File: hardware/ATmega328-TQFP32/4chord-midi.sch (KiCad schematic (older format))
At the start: 55 parts, among them IC1 ATMEGA328P-A, P1 USB_B, P2 Programmer, P3 UART, Q1 2N2222, SW1 Menu Minus, SW2 Menu Select, SW3 Menu Plus, SW4 Chord I, SW5 Chord V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

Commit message: issue-#13: Revised Revision B hardware
Reworked schematic to separate to logical blocks, added reset circuit,
fixed Q1 pin assignment and changed it from BJT to MOSFET component.
Also added power supply choices for UART (5V, 3.3V and none) and a
fourth rubber foot for better balance.

Obviously same changes in the PCB design, also moved button silk screen
bit more down for better readability. Fixed one sharp corner in the
board border. Improved routing somewhat.
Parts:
- removed Q1: 2N2222, TO_SOT_Packages_SMD:SOT-23, symbol Q_NPN_EBC
- removed R19, R20: 0R, Resistors_SMD:R_0805_HandSoldering, symbol R
- removed W1: TP, Pin_Headers:Pin_Header_Straight_1x01_Pitch2.54mm, symbol TEST_1P
- added C16: 100n, Capacitors_SMD:C_0805_HandSoldering, symbol C
- added P4: UART Power, Pin_Headers:Pin_Header_Straight_1x04_Pitch2.54mm, symbol CONN_01X04
- added Q1: 2N7002, TO_SOT_Packages_SMD:SOT-23, symbol Q_NMOS_GSD
- R16: value 1k -> 100
- R17: value 0R -> 1M
- R18: value 0R -> 10k
- SW1: value Menu Minus -> <
- SW2: value Menu Select -> Select
- SW3: value Menu Plus -> >
- SW4: value Chord I -> I
- SW5: value Chord V -> V
- SW6: value Chord vi -> vi
- SW7: value Chord IV -> IV
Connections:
- net labels added: +5V, BTN_MENU_NEXT, BTN_MENU_PREV
- net labels removed: BTN_MENU_MINUS, BTN_MENU_PLUS
- wire segments 166 -> 170
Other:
- note added: "Chord buttons"
- note added: "Clock"
- note added: "LCD / back light"
- note added: "Menu buttons"
- note added: "Power"
- note added: "Serial Programmer"
- note added: "UART"
- note added: "USB"
- moved on the sheet: C1, C10, C11, C12, C13, C14, C15, C2, C3, C4, C5, C6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

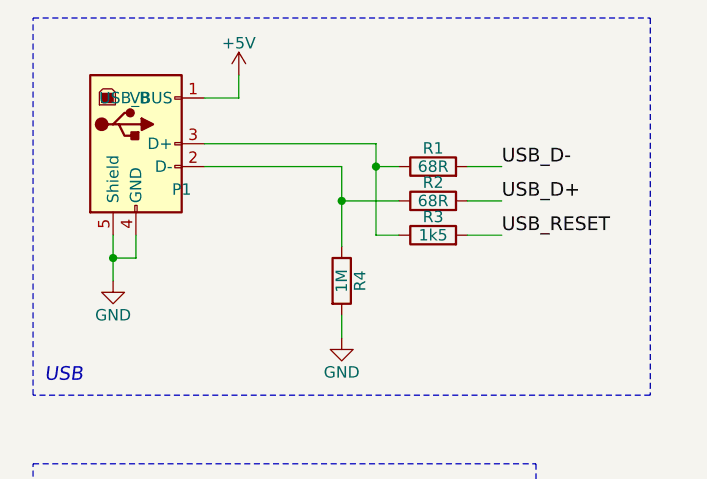
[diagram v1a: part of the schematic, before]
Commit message: Add schematic cache lib to repository
Otherwise it's just fucked up anyway since KiCad generates default
netlist now to reference the cache lib instead of the builtin
components. Probably best this way with changes happening now and then
in the builtin ones. Which I fixed here too, since someone had the grand
idea to change the USB-B component's pin arrangement to 1-3-2-4-5 and
swap D+ and D- order.
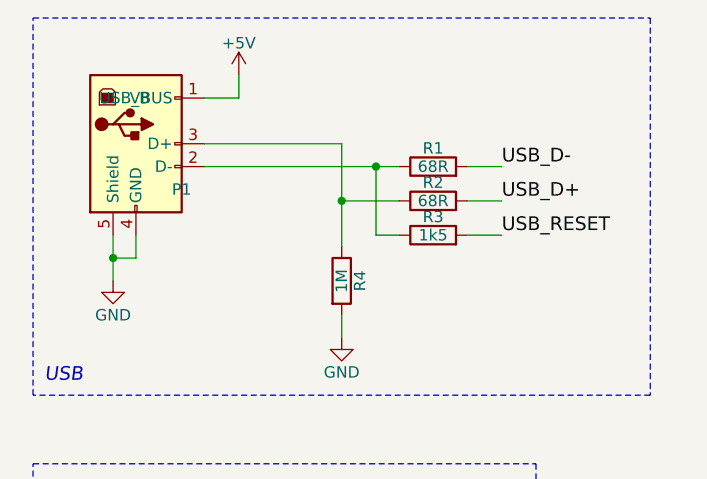
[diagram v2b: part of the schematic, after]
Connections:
- net at R2.1, R4.1: now also P1.3 (D+); no longer P1.2 (D-)
- net at R1.1, R3.1: now also P1.2 (D-); no longer P1.3 (D+)
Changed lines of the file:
@@
 Sheet 1 1
 Title "4chord MIDI ATmega328-TQFP32"
-Date "2017-08-05"
+Date "2017-09-12"
 Rev "B"
 Comp "Sven Gregori <sven@craplab.fi>"
@@
 	1    0    0    -1
 $EndComp
-Wire Wire Line
-	2050 1100 2050 1500
-Connection ~ 2050 1200
 Connection ~ 1050 2900
 Wire Wire Line
@@
 	1900 1350 2150 1350
 Wire Wire Line
-	1900 1200 1900 1550
-Wire Wire Line
-	2050 1200 2150 1200
+	1300 1200 2150 1200
 Connection ~ 1650 7100
 Connection ~ 1650 7200
@@
 	900  1600 1000 1600
 Wire Wire Line
-	1300 1100 2050 1100
-Wire Wire Line
-	1300 1200 1900 1200
+	2050 1500 2050 1200
+Connection ~ 2050 1200
+Wire Wire Line
+	1300 1100 1900 1100
+Wire Wire Line
+	1900 1100 1900 1550
 $EndSCHEMATC
